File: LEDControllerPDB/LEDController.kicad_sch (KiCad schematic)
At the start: 17 parts, among them J1 3557-2, J11 TB002-500-04BE, J12 TB002-500-04BE, J17 TB002-500-04BE, J2 3557-2, J3 3557-2, J4 3557-2, J5 3557-2, J6 3557-2, J7 0389690002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

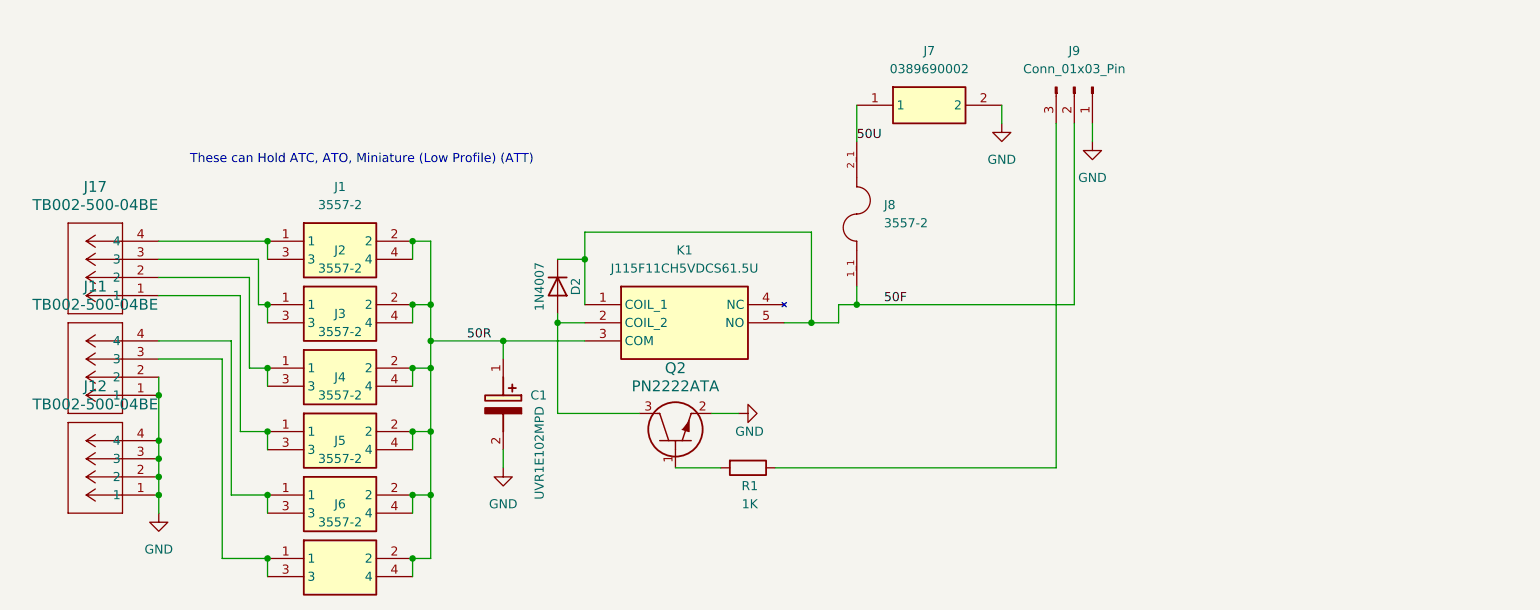
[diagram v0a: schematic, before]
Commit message: add 24v support and reverse voltage protection
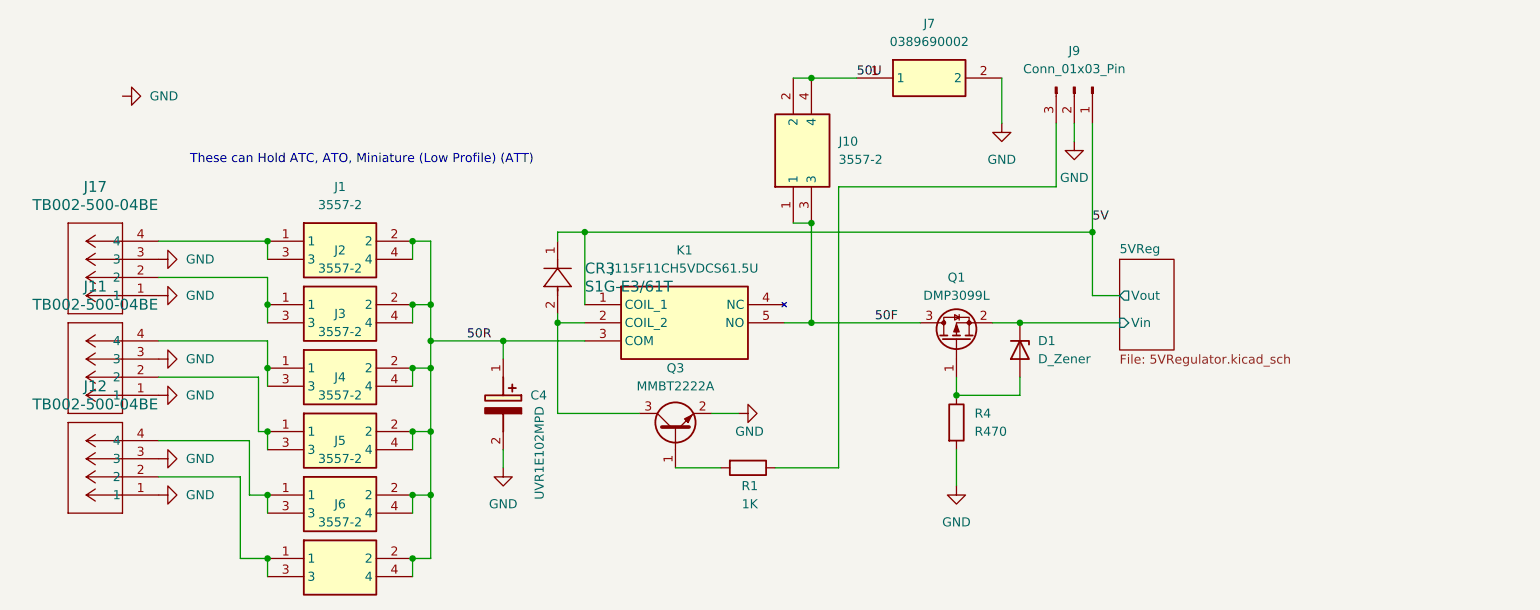
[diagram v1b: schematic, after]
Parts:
- removed D2: 1N4007, Diode_THT:D_DO-41_SOD81_P10.16mm_Horizontal, symbol Diode:1N4007
- removed J8: 3557-2, LEDController:FUSE_3555-2, symbol LEDController:3555-2
- removed Q2: PN2222ATA, TO-92_ONS, symbol LEDController:PN2222ATA
- added CR3: S1G-E3/61T, DIODE_DO214AC, symbol LEDController:S1G-E3_61T
- added D1: D_Zener, Diode_SMD:D_SOD-123, symbol Device:D_Zener
- added J10: 3557-2, 3557-2, symbol LEDController:3557-2
- added Q1: DMP3099L, Package_TO_SOT_SMD:SOT-23-3, symbol Transistor_FET:DMP3099L
- added Q3: MMBT2222A, Package_TO_SOT_SMD:SOT-23, symbol Transistor_BJT:MMBT2222A
- added R4: R470, Resistor_SMD:R_0201_0603Metric_Pad0.64x0.40mm_HandSolder, symbol Device:R
- R1: footprint Resistor_THT:R_Axial_DIN0309_L9.0mm_D3.2mm_P12.70mm_Horizontal -> Resistor_SMD:R_0603_1608Metric_Pad0.98x0.95mm_HandSolder
- renumbered C1 to C4
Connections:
- net 50F: now also J10.1, J10.3, Q1.3 (D); no longer J9.2 (Pin_2), K1.1 (COIL_1)
- net 50U: now also J10.2, J10.4
- net GND: now also J11.3, J17.1, J17.3, J9.2 (Pin_2), Q3.2 (E), R4.2; no longer J11.2, J12.2, J12.4, J9.1 (Pin_1)
- net at J2.1, J2.3: now also J17.2; no longer J17.3
- net at K1.2 (COIL_2): now also CR3.2, Q3.3 (C)
- net at J6.1, J6.3: now also J12.2; no longer J11.3
- net at R1.2: now also Q3.1 (B)
- net at J4.1, J4.3: now also J11.2; no longer J17.1
- net at J3.1, J3.3: now also J11.4; no longer J17.2
- net at J5.1, J5.3: now also J12.4; no longer J11.4
- new net: D1.2 (A), Q1.1 (G), R4.1
- new net 5V: CR3.1, J9.1 (Pin_1), K1.1 (COIL_1)
- new net 5VReg/Vin: D1.1 (K), Q1.2 (S)
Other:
- added sheet 5VReg (5VRegulator.kicad_sch)
- moved on the sheet: J7

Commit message: rerout
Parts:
- R4: value R470 -> 470
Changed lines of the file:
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@@
 	)
 	(label "50F"
-		(at 139.7 62.23 0)
+		(at 135.89 62.23 0)
 		(fields_autoplaced yes)
 		(effects
@@
 		)
 		(property "50F" ""
-			(at 139.7 63.5 0)
+			(at 135.89 63.5 0)
 			(effects
 				(font
@@
 			)
 		)
-		(property "Value" "R470"
+		(property "Value" "470"
 			(at 153.67 77.4699 0)
 			(effects

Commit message: hand solder
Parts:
- R4: footprint Resistor_SMD:R_0201_0603Metric_Pad0.64x0.40mm_HandSolder -> Resistor_SMD:R_0603_1608Metric_Pad0.98x0.95mm_HandSolder
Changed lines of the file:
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@@
 			)
 		)
-		(property "Footprint" "Resistor_SMD:R_0201_0603Metric_Pad0.64x0.40mm_HandSolder"
+		(property "Footprint" "Resistor_SMD:R_0603_1608Metric_Pad0.98x0.95mm_HandSolder"
 			(at 149.352 76.2 90)
 			(effects

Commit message: done
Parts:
- removed J7: 0389690002, 0389690002, symbol LEDController:0389690002
- removed J9: Conn_01x03_Pin, Connector_PinSocket_2.54mm:PinSocket_1x03_P2.54mm_Vertical, symbol Connector:Conn_01x03_Pin
- removed R1: 1K, Resistor_SMD:R_0603_1608Metric_Pad0.98x0.95mm_HandSolder, symbol Device:R
- added J13: 647676-3, LEDController:TE_647676-3, symbol LEDController:647676-3
- added J7: Conn_02x02_Row_Letter_First, Connector_PinHeader_2.54mm:PinHeader_2x02_P2.54mm_Vertical, symbol Connector_Generic:Conn_02x02_Counter_Clockwise
- added J8: HB9500-9.5-2P, SHDR2W140P0X950_1X2_2055X1800X1440P, symbol LEDController:HB9500-9.5-2P
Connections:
- net 50U: now also J8.1
- net 5V: now also J13.3, J7.3 (Pin_3)
- net 5VReg/Vin: now also J7.4 (Pin_4); no longer D1.1 (K), Q1.2 (S)
- net GND: now also J13.2, J8.2
- net Relay Controll: now reaches Q3.1 (B)
- net Relay Controll: now also J13.1
- new net: D1.1 (K), J7.1 (Pin_1), J7.2 (Pin_2), Q1.2 (S)

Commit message: generate outputs
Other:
- note added: "Reverse Current Protection"
- title: (none) -> LED Power Distribution Board
- moved on the sheet: J7
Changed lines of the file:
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@@
 	(generator_version "9.0")
 	(paper "A4")
+	(title_block
+		(title "LED Power Distribution Board")
+		(date "2025-04-18")
+		(rev "02")
+	)
+	(rectangle
+		(start 142.24 50.8)
+		(end 170.18 92.71)
+		(stroke
+			(width 0)
+			(type default)
+		)
+		(fill
+			(type none)
+		)
+	)
+	(text "Reverse Current Protection"
+		(exclude_from_sim no)
+		(at 156.464 52.324 0)
+		(effects
+			(font
+				(size 1.27 1.27)
+			)
+		)
+	)
 	(text "These can Hold ATC, ATO, Miniature (Low Profile) (ATT)"
 		(exclude_from_sim no)
@@
 	)
 	(junction
-		(at 185.42 57.15)
+		(at 193.04 57.15)
 		(diameter 0)
 		(color 0 0 0 0)
@@
 	)
 	(junction
-		(at 171.45 62.23)
+		(at 179.07 62.23)
 		(diameter 0)
 		(color 0 0 0 0)
@@
 	(wire
 		(pts
-			(xy 187.96 62.23) (xy 190.5 62.23)
+			(xy 195.58 62.23) (xy 198.12 62.23)
 		)
 		(stroke
@@
 	(wire
 		(pts
-			(xy 170.18 49.53) (xy 170.18 57.15)
+			(xy 177.8 49.53) (xy 177.8 57.15)
 		)
 		(stroke
@@
 	(wire
 		(pts
-			(xy 185.42 57.15) (xy 190.5 57.15)
+			(xy 193.04 57.15) (xy 198.12 57.15)
 		)
 		(stroke
@@
 	(wire
 		(pts
-			(xy 95.25 60.96) (xy 95.25 62.23)
+			(xy 160.02 62.23) (xy 179.07 62.23)
 		)
 		(stroke
@@
 	(wire
 		(pts
-			(xy 185.42 57.15) (xy 185.42 62.23)
+			(xy 95.25 60.96) (xy 95.25 62.23)
 		)
 		(stroke
@@
 	(wire
 		(pts
-			(xy 187.96 59.69) (xy 187.96 62.23)
+			(xy 193.04 57.15) (xy 193.04 62.23)
 		)
 		(stroke
@@
 	(wire
 		(pts
-			(xy 160.02 62.23) (xy 171.45 62.23)
+			(xy 195.58 59.69) (xy 195.58 62.23)
 		)
 		(stroke
@@
 	(wire
 		(pts
-			(xy 184.15 62.23) (xy 185.42 62.23)
+			(xy 191.77 62.23) (xy 193.04 62.23)
 		)
 		(stroke
@@
 	(wire
 		(pts
-			(xy 184.15 59.69) (xy 187.96 59.69)
+			(xy 191.77 59.69) (xy 195.58 59.69)
 		)
 		(stroke
@@
 	(wire
 		(pts
+			(xy 177.8 49.53) (xy 170.18 49.53)
+		)
+		(stroke
+			(width 0)
+			(type default)
+		)
+	)
+	(wire
+		(pts
 			(xy 111.76 82.55) (xy 134.62 82.55)
 		)
@@
 	(wire
 		(pts
-			(xy 171.45 59.69) (xy 171.45 62.23)
+			(xy 179.07 59.69) (xy 179.07 62.23)
 		)
 		(stroke
@@
 	(wire
 		(pts
-			(xy 170.18 57.15) (xy 185.42 57.15)
+			(xy 177.8 57.15) (xy 193.04 57.15)
 		)
 		(stroke
@@
 	)
 	(label "5V"
-		(at 170.18 53.34 0)
+		(at 177.8 53.34 0)
 		(effects
 			(font
@@
 	)
 	(symbol
-		(lib_id "power:GND")
-		(at 34.29 30.48 90)
-		(unit 1)
-		(exclude_from_sim no)
-		(in_bom yes)
-		(on_board yes)
-		(dnp no)
-		(fields_autoplaced yes)
-		(property "Reference" "#PWR01"
-			(at 40.64 30.48 0)
-			(effects
-				(font
-					(size 1.27 1.27)
-				)
-				(hide yes)
-			)
-		)
-		(property "Value" "GND"
-			(at 38.1 30.4799 90)
-			(effects
-				(font
-					(size 1.27 1.27)
-				)
-				(justify right)
-			)
-		)
-		(property "Footprint" ""
-			(at 34.29 30.48 0)
-			(effects
-				(font
-					(size 1.27 1.27)
-				)
-				(hide yes)
-			)
-		)
-		(property "Datasheet" ""
-			(at 34.29 30.48 0)
-			(effects
-				(font
-					(size 1.27 1.27)
-				)
-				(hide yes)
-			)
-		)
-		(property "Description" "Power symbol creates a global label with name \"GND\" , ground"
-			(at 34.29 30.48 0)
-			(effects
-				(font
-					(size 1.27 1.27)
-				)
-				(hide yes)
-			)
-		)
-		(pin "1"
-		)
-		(instances
-			(project ""
-				(path "/62aa0f20-cf9c-44ed-8f8b-d852f912cf95"
-					(reference "#PWR01")
-					(unit 1)
-				)
-			)
-		)
-	)
-	(symbol
 		(lib_id "Transistor_BJT:MMBT2222A")
 		(at 111.76 77.47 90)
@@
 	(symbol
 		(lib_id "Connector_Generic:Conn_02x02_Counter_Clockwise")
-		(at 176.53 59.69 0)
+		(at 184.15 59.69 0)
 		(unit 1)
 		(exclude_from_sim no)
@@
 		(on_board yes)
 		(dnp no)
-		(fields_autoplaced yes)
 		(property "Reference" "J7"
-			(at 177.8 53.34 0)
+			(at 185.166 64.77 0)
 			(effects
 				(font
@@
 		)
 		(property "Value" "Conn_02x02_Row_Letter_First"
-			(at 177.8 55.88 0)
+			(at 185.166 67.31 0)
 			(effects
 				(font
@@
 		)
 		(property "Footprint" "Connector_PinHeader_2.54mm:PinHeader_2x02_P2.54mm_Vertical"
-			(at 176.53 59.69 0)
+			(at 184.15 59.69 0)
 			(effects
 				(font
@@
 		)
 		(property "Datasheet" "~"
-			(at 176.53 59.69 0)
+			(at 184.15 59.69 0)
 			(effects
 				(font
@@
 		)
 		(property "Description" "Generic connector, double row, 02x02, counter clockwise pin numbering scheme (similar to DIP package numbering), script generated (kicad-library-utils/schlib/autogen/connector/)"
-			(at 176.53 59.69 0)
+			(at 184.15 59.69 0)
 			(effects
 				(font
@@
 	)
 	(sheet
-		(at 190.5 53.34)
+		(at 198.12 53.34)
 		(size 7.62 12.7)
 		(exclude_from_sim no)
@@
 		(on_board yes)
 		(dnp no)
-		(fields_autoplaced yes)
 		(stroke
 			(width 0.1524)
@@
 		)
 		(property "Sheetname" "5VReg"
-			(at 190.5 52.6284 0)
+			(at 198.12 52.6284 0)
 			(effects
 				(font
@@
 		)
 		(property "Sheetfile" "5VRegulator.kicad_sch"
-			(at 190.5 66.6246 0)
+			(at 198.12 49.022 0)
 			(effects
 				(font
@@
 		)
 		(pin "Vin" input
-			(at 190.5 62.23 180)
+			(at 198.12 62.23 180)
 			(effects
 				(font
@@
 		)
 		(pin "Vout" output
-			(at 190.5 57.15 180)
+			(at 198.12 57.15 180)
 			(effects
 				(font
